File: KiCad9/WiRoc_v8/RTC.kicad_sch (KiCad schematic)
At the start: 8 parts, among them U4 74LS73, U9 PCF8563T, Y1 32.768kHz

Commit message: etc
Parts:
- C13, C19: LCSC Part # C15849 -> C52923; ManufacturerPartNumber CL10A105KB8NNNC -> CL05A105KA5NQNC
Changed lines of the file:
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@@
 			)
 		)
-		(property "Datasheet" "https://jlcpcb.com/partdetail/16531-CL10A105KB8NNNC/C15849"
+		(property "Datasheet" "https://jlcpcb.com/api/file/downloadByFileSystemAccessId/8579707174974914560"
 			(at 181.61 86.36 0)
 			(effects
@@
 			)
 		)
-		(property "LCSC Part #" "C15849"
+		(property "LCSC Part #" "C52923"
 			(at 181.61 86.36 0)
 			(effects
@@
 			)
 		)
-		(property "ManufacturerPartNumber" "CL10A105KB8NNNC"
+		(property "ManufacturerPartNumber" "CL05A105KA5NQNC"
 			(at 181.61 86.36 0)
 			(effects
@@
 			)
 		)
-		(property "Datasheet" "https://jlcpcb.com/partdetail/16531-CL10A105KB8NNNC/C15849"
+		(property "Datasheet" "https://jlcpcb.com/api/file/downloadByFileSystemAccessId/8579707174974914560"
 			(at 90.17 64.77 0)
 			(effects
@@
 			)
 		)
-		(property "LCSC Part #" "C15849"
+		(property "LCSC Part #" "C52923"
 			(at 90.17 64.77 0)
 			(effects
@@
 			)
 		)
-		(property "ManufacturerPartNumber" "CL10A105KB8NNNC"
+		(property "ManufacturerPartNumber" "CL05A105KA5NQNC"
 			(at 90.17 64.77 0)
 			(effects

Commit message: add bom
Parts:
- C12, Y1: JLCBasicExtended (none) -> Basic
- C13, C19: JLCBasicExtended (none) -> Basic; Package 0603 -> 0402
- R17, R7: JLCBasicExtended (none) -> Basic; LCSC Part # C25811 -> C25764; ManufacturerPartNumber 0603WAF2003T5E -> 0402WGF2003TCE; Package 0603 -> 0402
- U4: JLCBasicExtended (none) -> Extended
- U9: JLCBasicExtended (none) -> Extended; Package (none) -> SO-8
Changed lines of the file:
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@@
+			)
+		)
+		(property "JLCBasicExtended" "Extended"
+			(at 180.34 38.1 0)
+			(effects
+				(font
+					(size 1.27 1.27)
+				)
+				(hide yes)
 			)
 		)
@@
 			)
 		)
+		(property "JLCBasicExtended" "Extended"
+			(at 171.45 68.58 0)
+			(effects
+				(font
+					(size 1.27 1.27)
+				)
+				(hide yes)
+			)
+		)
 		(pin "10"
 		)
@@
 			)
 		)
+		(property "JLCBasicExtended" "Basic"
+			(at 101.6 76.2 0)
+			(effects
+				(font
+					(size 1.27 1.27)
+				)
+				(hide yes)
+			)
+		)
 		(pin "1"
 		)
@@
 			)
 		)
+		(property "JLCBasicExtended" "Extended"
+			(at 124.46 63.5 0)
+			(effects
+				(font
+					(size 1.27 1.27)
+				)
+				(hide yes)
+			)
+		)
+		(property "Package" "SO-8"
+			(at 124.46 63.5 0)
+			(effects
+				(font
+					(size 1.27 1.27)
+				)
+				(hide yes)
+			)
+		)
 		(pin "1"
 		)
@@
 			)
 		)
-		(property "LCSC Part #" "C25811"
+		(property "LCSC Part #" "C25764"
 			(at 181.61 76.2 0)
 			(effects
@@
 			)
 		)
-		(property "ManufacturerPartNumber" "0603WAF2003T5E"
+		(property "ManufacturerPartNumber" "0402WGF2003TCE"
 			(at 181.61 76.2 0)
 			(effects
@@
 			)
 		)
-		(property "Package" "0603"
+		(property "Package" "0402"
 			(at 181.61 76.2 0)
 			(effects
@@
 		)
 		(property "WebsiteURL" "https://lcsc.com/product-detail/Chip-Resistor-Surface-Mount-UniOhm_Uniroyal-Elec-0603WAF2003T5E_C25811.html"
+			(at 181.61 76.2 0)
+			(effects
+				(font
+					(size 1.27 1.27)
+				)
+				(hide yes)
+			)
+		)
+		(property "JLCBasicExtended" "Basic"
 			(at 181.61 76.2 0)
 			(effects
@@
 			)
 		)
+		(property "JLCBasicExtended" "Extended"
+			(at 161.29 39.37 0)
+			(effects
+				(font
+					(size 1.27 1.27)
+				)
+				(hide yes)
+			)
+		)
 		(pin "10"
 		)
@@
 			)
 		)
+		(property "JLCBasicExtended" "Basic"
+			(at 106.68 68.58 0)
+			(effects
+				(font
+					(size 1.27 1.27)
+				)
+				(hide yes)
+			)
+		)
 		(pin "1"
 		)
@@
 			)
 		)
-		(property "Package" "0603"
+		(property "Package" "0402"
 			(at 181.61 86.36 0)
 			(effects
@@
 		)
 		(property "ThroughHole" "FALSE"
+			(at 181.61 86.36 0)
+			(effects
+				(font
+					(size 1.27 1.27)
+				)
+				(hide yes)
+			)
+		)
+		(property "JLCBasicExtended" "Basic"
 			(at 181.61 86.36 0)
 			(effects
@@
 			)
 		)
-		(property "Package" "0603"
+		(property "Package" "0402"
 			(at 90.17 64.77 0)
 			(effects
@@
 		)
 		(property "ThroughHole" "FALSE"
+			(at 90.17 64.77 0)
+			(effects
+				(font
+					(size 1.27 1.27)
+				)
+				(hide yes)
+			)
+		)
+		(property "JLCBasicExtended" "Basic"
 			(at 90.17 64.77 0)
 			(effects
@@
 			)
 		)
-		(property "LCSC Part #" "C25811"
+		(property "LCSC Part #" "C25764"
 			(at 139.7 72.39 0)
 			(effects
@@
 			)
 		)
-		(property "ManufacturerPartNumber" "0603WAF2003T5E"
+		(property "ManufacturerPartNumber" "0402WGF2003TCE"
 			(at 139.7 72.39 0)
 			(effects
@@
 			)
 		)
-		(property "Package" "0603"
+		(property "Package" "0402"
 			(at 139.7 72.39 0)
 			(effects
@@
 			(at 139.7 72.39 0)
 			(effects
+				(font
+					(size 1.27 1.27)
+				)
+				(hide yes)
+			)
+		)
+		(property "JLCBasicExtended" "Basic"
+			(at 139.7 72.39 0)
+			(effects

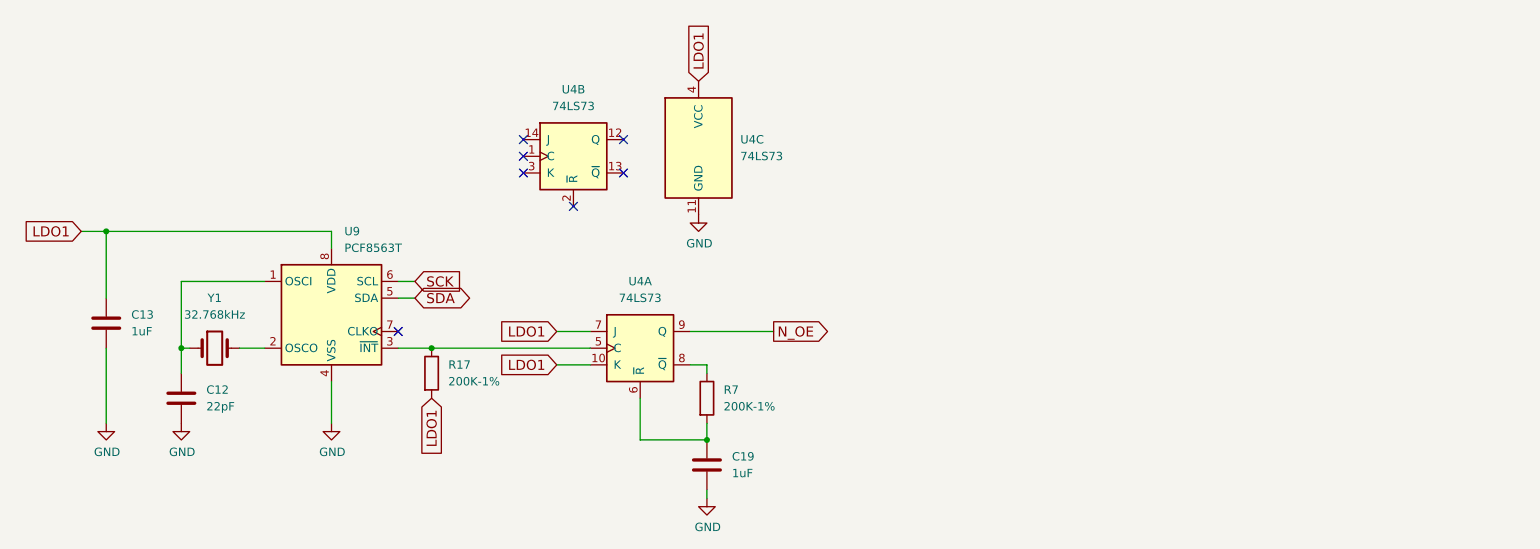
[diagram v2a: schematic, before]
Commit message: add esp32hosted-c5 board
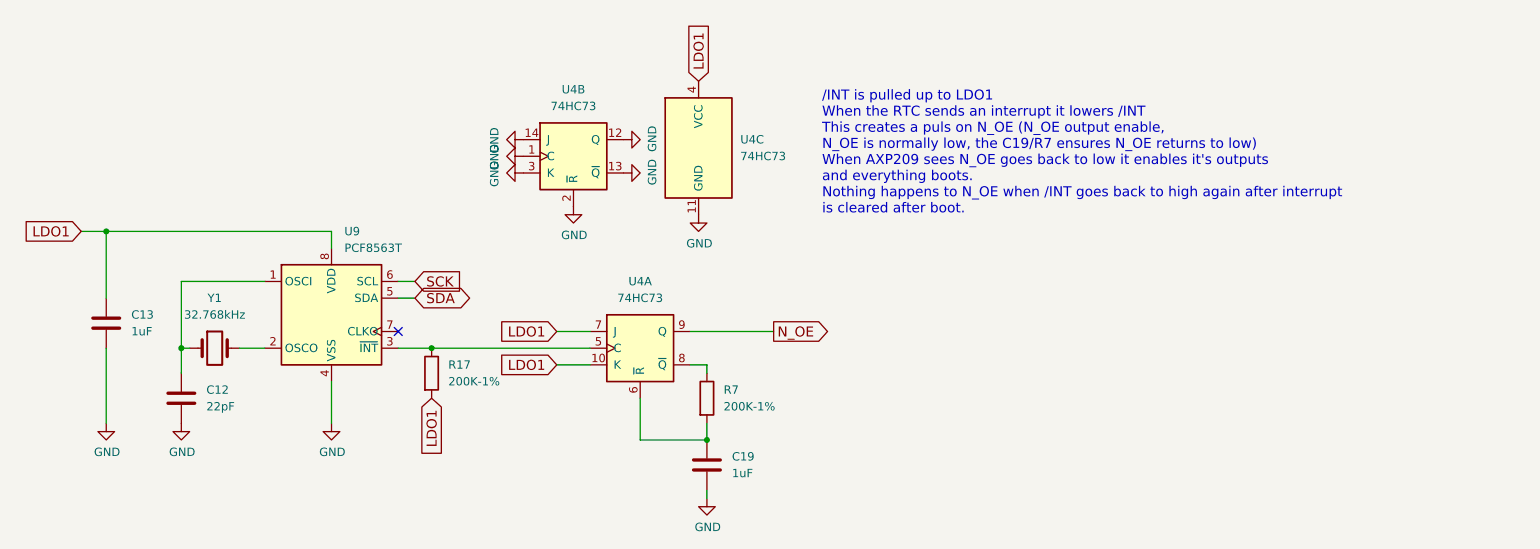
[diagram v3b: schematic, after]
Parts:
- U4: value 74LS73 -> 74HC73
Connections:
- net GND: now also U4.1 (C), U4.12 (Q), U4.13 (~{Q}), U4.14 (J), U4.2 (~{R}), U4.3 (K)
- no-connect marks 7 -> 1
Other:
- note added: "/INT is pulled up to LDO1 When the RTC sends an interrupt it lowers /INT This creates a puls on N_OE (N_OE output enable, N_OE is normally low, the C19/R7 ensures N_OE returns to low) When AXP209 sees N_OE goes back to low it enables it's outputs and everything boots. Nothing happens to N_OE when /INT goes back to high again after interrupt is cleared after boot."

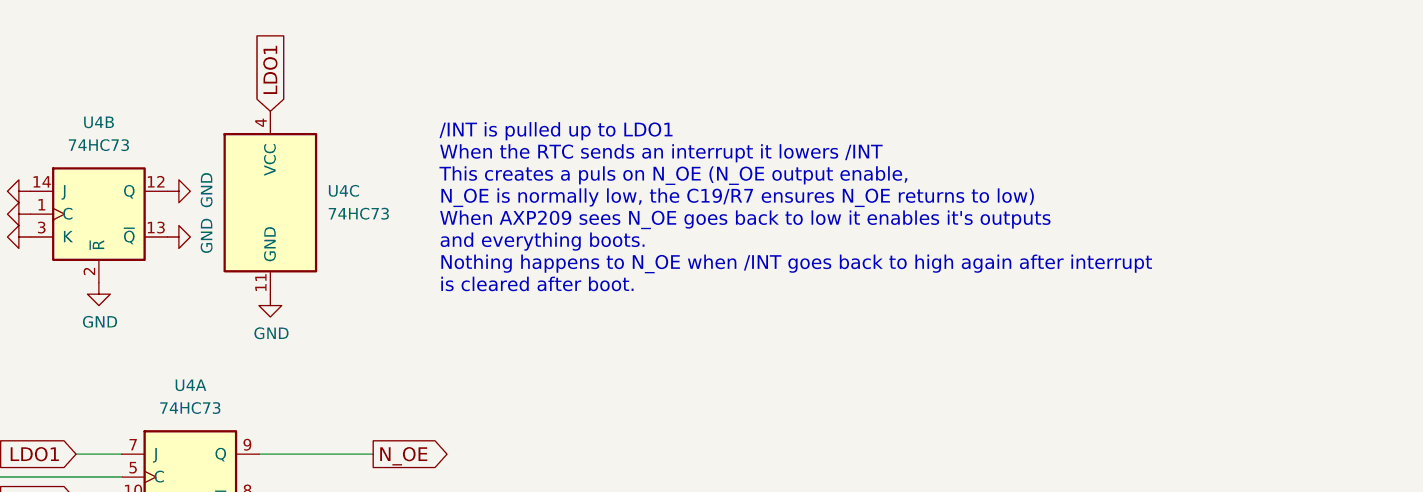
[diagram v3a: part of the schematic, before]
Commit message: change to 10uF in pdn, vdd-dram area to south caps, remove varistor, etc
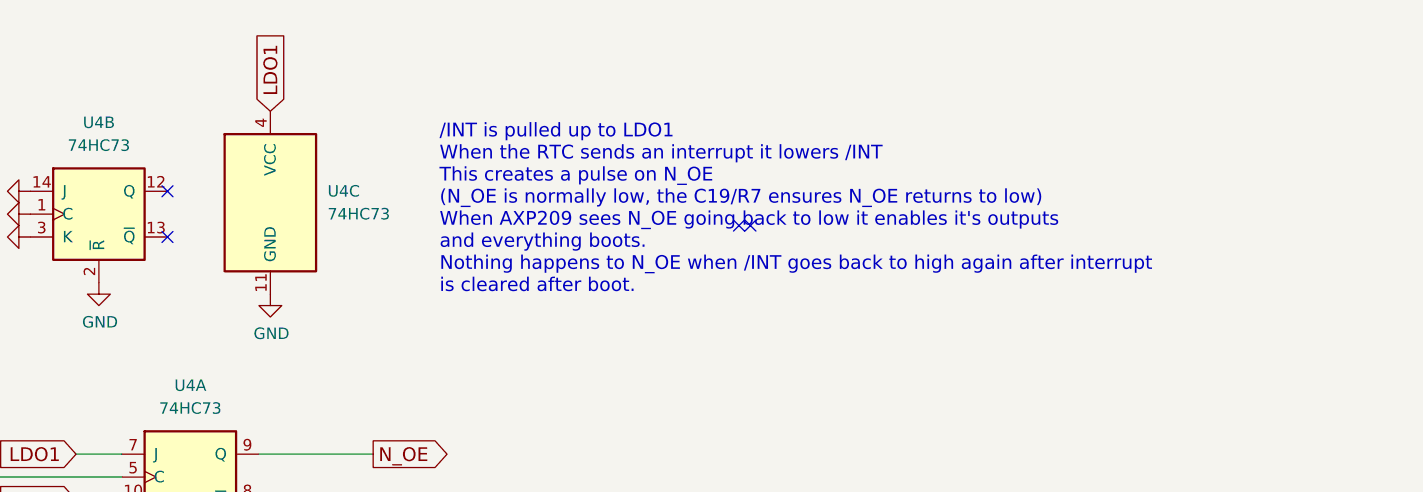
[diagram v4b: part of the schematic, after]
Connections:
- net GND: no longer U4.12 (Q), U4.13 (~{Q})
- no-connect marks 1 -> 5
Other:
- note added: "/INT is pulled up to LDO1 When the RTC sends an interrupt it lowers /INT This creates a pulse on N_OE (N_OE is normally low, the C19/R7 ensures N_OE returns to low) When AXP209 sees N_OE going back to low it enables it's outputs and everything boots. Nothing happens to N_OE when /INT goes back to high again after interrupt is cleared after boot."
- note removed: "/INT is pulled up to LDO1 When the RTC sends an interrupt it lowers /INT This creates a puls on N_OE (N_OE output enable, N_OE is normally low, the C19/R7 ensures N_OE returns to low) When AXP209 sees N_OE goes back to low it enables it's outputs and everything boots. Nothing happens to N_OE when /INT goes back to high again after interrupt is cleared after boot."
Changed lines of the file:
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@@
 	(generator_version "9.0")
 	(paper "A4")
-	(text "/INT is pulled up to LDO1\nWhen the RTC sends an interrupt it lowers /INT\nThis creates a puls on N_OE (N_OE output enable, \nN_OE is normally low, the C19/R7 ensures N_OE returns to low)\nWhen AXP209 sees N_OE goes back to low it enables it's outputs\nand everything boots.\nNothing happens to N_OE when /INT goes back to high again after interrupt\nis cleared after boot."
+	(text "/INT is pulled up to LDO1\nWhen the RTC sends an interrupt it lowers /INT\nThis creates a pulse on N_OE \n(N_OE is normally low, the C19/R7 ensures N_OE returns to low)\nWhen AXP209 sees N_OE going back to low it enables it's outputs\nand everything boots.\nNothing happens to N_OE when /INT goes back to high again after interrupt\nis cleared after boot."
 		(exclude_from_sim no)
 		(at 199.136 38.862 0)
@@
 		(diameter 0)
 		(color 0 0 0 0)
+	)
+	(no_connect
+		(at 168.91 41.91)
+	)
+	(no_connect
+		(at 232.41 40.64)
+	)
+	(no_connect
+		(at 168.91 36.83)
+	)
+	(no_connect
+		(at 233.68 40.64)
 	)
 	(no_connect
@@
 	)
 	(symbol
-		(lib_id "power:GND")
-		(at 168.91 41.91 90)
-		(unit 1)
-		(exclude_from_sim no)
-		(in_bom yes)
-		(on_board yes)
-		(dnp no)
-		(property "Reference" "#PWR0115"
-			(at 175.26 41.91 0)
-			(effects
-				(font
-					(size 1.27 1.27)
-				)
-				(hide yes)
-			)
-		)
-		(property "Value" "GND"
-			(at 173.3042 41.783 0)
-			(effects
-				(font
-					(size 1.27 1.27)
-				)
-			)
-		)
-		(property "Footprint" ""
-			(at 168.91 41.91 0)
-			(effects
-				(font
-					(size 1.27 1.27)
-				)
-				(hide yes)
-			)
-		)
-		(property "Datasheet" ""
-			(at 168.91 41.91 0)
-			(effects
-				(font
-					(size 1.27 1.27)
-				)
-				(hide yes)
-			)
-		)
-		(property "Description" ""
-			(at 168.91 41.91 0)
-			(effects
-				(font
-					(size 1.27 1.27)
-				)
-				(hide yes)
-			)
-		)
-		(pin "1"
-		)
-		(instances
-			(project "WiRoc_NanoPi"
-				(path "/8ba0b499-eaca-4cd5-a002-c6bdb610cc8c/420ce888-9e08-49fd-b3f8-96e9de814cbc"
-					(reference "#PWR0115")
-					(unit 1)
-				)
-			)
-		)
-	)
-	(symbol
 		(lib_id "74xx:74LS73")
 		(at 171.45 68.58 0)
@@
 					(unit 1)
 				)
-			)
-		)
-	)
-	(symbol
-		(lib_id "power:GND")
-		(at 168.91 36.83 90)
-		(unit 1)
-		(exclude_from_sim no)
-		(in_bom yes)
-		(on_board yes)
-		(dnp no)
-		(property "Reference" "#PWR0117"
-			(at 175.26 36.83 0)
-			(effects
-				(font
-					(size 1.27 1.27)
-				)
-				(hide yes)
-			)
-		)
-		(property "Value" "GND"
-			(at 173.3042 36.703 0)
-			(effects
-				(font
-					(size 1.27 1.27)
-				)
-			)
-		)
-		(property "Footprint" ""
-			(at 168.91 36.83 0)
-			(effects
-				(font
-					(size 1.27 1.27)
-				)
-				(hide yes)
-			)
-		)
-		(property "Datasheet" ""
-			(at 168.91 36.83 0)
-			(effects
-				(font
-					(size 1.27 1.27)
-				)
-				(hide yes)
-			)
-		)
-		(property "Description" ""
-			(at 168.91 36.83 0)
-			(effects
-				(font
-					(size 1.27 1.27)
-				)
-				(hide yes)
-			)
-		)
-		(pin "1"
-		)
-		(instances
-			(project "WiRoc_NanoPi"
-				(path "/8ba0b499-eaca-4cd5-a002-c6bdb610cc8c/420ce888-9e08-49fd-b3f8-96e9de814cbc"
-					(reference "#PWR0117")
-					(unit 1)
-				)

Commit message: many small changes, change eMMC
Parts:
- C12: Manufacturer Murata Electronics -> FH (Guangdong Fenghua Advanced Tech); ManufacturerPartNumber GRM155R71C223JA01D -> 0402CG220J500NT
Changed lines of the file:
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@@
 			)
 		)
-		(property "Manufacturer" "Murata Electronics"
+		(property "Manufacturer" "FH (Guangdong Fenghua Advanced Tech)"
 			(at 101.6 76.2 0)
 			(effects
@@
 			)
 		)
-		(property "ManufacturerPartNumber" "GRM155R71C223JA01D"
+		(property "ManufacturerPartNumber" "0402CG220J500NT"
 			(at 101.6 76.2 0)
 			(effects

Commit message: etc
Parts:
- U4, U9: JLCPCB Rotation Offset -90 -> (none)
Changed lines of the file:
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@@
 			)
 		)
-		(property "JLCPCB Rotation Offset" "-90"
+		(property "JLCBasicExtended" "Extended"
 			(at 180.34 38.1 0)
 			(effects
@@
 			)
 		)
-		(property "JLCBasicExtended" "Extended"
+		(property "FT Rotation Offset" ""
 			(at 180.34 38.1 0)
 			(effects
@@
 			)
 		)
-		(property "JLCPCB Rotation Offset" "-90"
-			(at 171.45 68.58 0)
-			(effects
-				(font
-					(size 1.27 1.27)
-				)
-				(hide yes)
-			)
-		)
 		(property "JLCBasicExtended" "Extended"
+			(at 171.45 68.58 0)
+			(effects
+				(font
+					(size 1.27 1.27)
+				)
+				(hide yes)
+			)
+		)
+		(property "FT Rotation Offset" ""
 			(at 171.45 68.58 0)
 			(effects
@@
 			)
 		)
-		(property "JLCPCB Rotation Offset" "-90"
-			(at 124.46 63.5 0)
-			(effects
-				(font
-					(size 1.27 1.27)
-				)
-				(hide yes)
-			)
-		)
 		(property "JLCBasicExtended" "Extended"
 			(at 124.46 63.5 0)
@@
 		)
 		(property "Package" "SO-8"
+			(at 124.46 63.5 0)
+			(effects
+				(font
+					(size 1.27 1.27)
+				)
+				(hide yes)
+			)
+		)
+		(property "FT Rotation Offset" ""
 			(at 124.46 63.5 0)
 			(effects
@@
 			)
 		)
-		(property "JLCPCB Rotation Offset" "-90"
-			(at 161.29 39.37 0)
-			(effects
-				(font
-					(size 1.27 1.27)
-				)
-				(hide yes)
-			)
-		)
 		(property "JLCBasicExtended" "Extended"
 			(at 161.29 39.37 0)
 			(effects
+				(font
+					(size 1.27 1.27)
+				)
+				(hide yes)
+			)
+		)
+		(property "FT Rotation Offset" ""
+			(at 161.29 39.37 0)
+			(effects
